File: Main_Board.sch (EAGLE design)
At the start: 52 parts, among them U1 RN4020RN4020, Y1 32KHz, Y2 25MHz

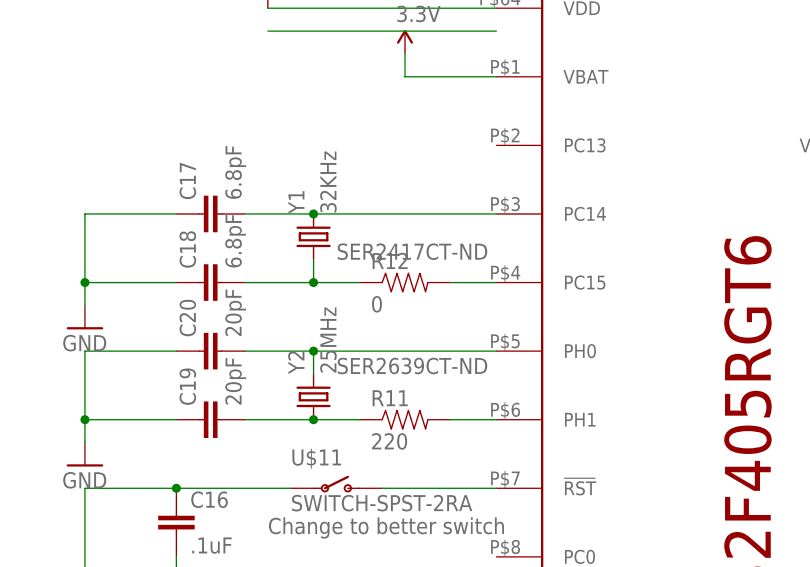
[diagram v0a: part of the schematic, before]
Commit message: added extra oscillator resistor
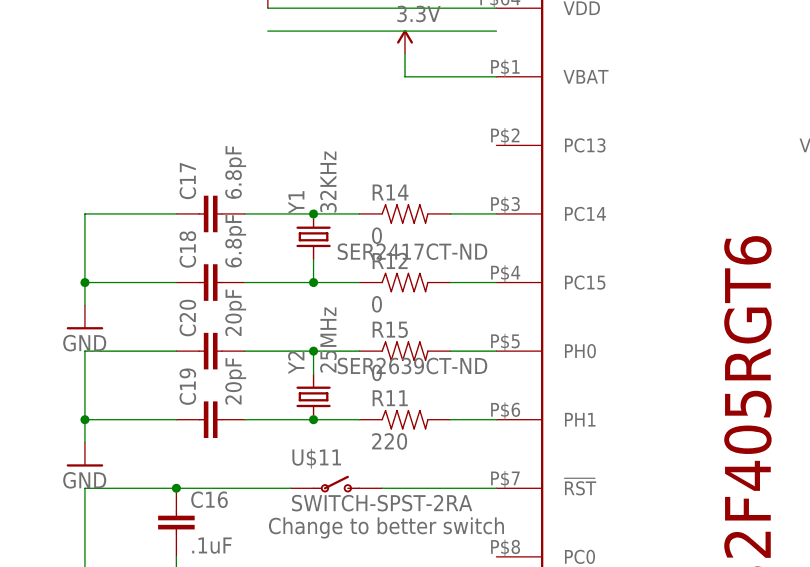
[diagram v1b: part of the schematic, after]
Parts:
- added R14, R15: 0, SparkFun-Passives:RESISTOR0805-RES
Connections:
- new net N$29: R14.2, U$5.PC14
- new net N$30: R15.2, U$5.PH0
- net N$12: now also R14.1; no longer U$5.PC14
- net N$20: now also R15.1; no longer U$5.PH0
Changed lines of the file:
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@@
 <part name="SUPPLY19" library="SparkFun-Aesthetics" deviceset="3.3V" device=""/>
 <part name="GND36" library="SparkFun-Aesthetics" deviceset="GND" device=""/>
+<part name="R14" library="SparkFun-Passives" deviceset="RESISTOR" device="0805-RES" value="0"/>
+<part name="R15" library="SparkFun-Passives" deviceset="RESISTOR" device="0805-RES" value="0"/>
 </parts>
 <sheets>
@@
 <instance part="SUPPLY19" gate="G$1" x="304.8" y="187.96"/>
 <instance part="GND36" gate="1" x="304.8" y="172.72"/>
+<instance part="R14" gate="G$1" x="325.12" y="127"/>
+<instance part="R15" gate="G$1" x="325.12" y="111.76"/>
 </instances>
 <busses>
@@
 <segment>
 <pinref part="Y1" gate="G$1" pin="2"/>
-<pinref part="U$5" gate="G$1" pin="PC14"/>
-<wire x1="314.96" y1="127" x2="335.28" y2="127" width="0.1524" layer="91"/>
 <pinref part="C17" gate="G$1" pin="2"/>
 <wire x1="307.34" y1="127" x2="314.96" y2="127" width="0.1524" layer="91"/>
+<pinref part="R14" gate="G$1" pin="1"/>
+<wire x1="314.96" y1="127" x2="320.04" y2="127" width="0.1524" layer="91"/>
 <junction x="314.96" y="127"/>
 </segment>
@@
 <segment>
 <pinref part="C20" gate="G$1" pin="2"/>
-<pinref part="U$5" gate="G$1" pin="PH0"/>
 <wire x1="307.34" y1="111.76" x2="314.96" y2="111.76" width="0.1524" layer="91"/>
 <pinref part="Y2" gate="G$1" pin="2"/>
-<wire x1="314.96" y1="111.76" x2="335.28" y2="111.76" width="0.1524" layer="91"/>
 <wire x1="314.96" y1="109.22" x2="314.96" y2="111.76" width="0.1524" layer="91"/>
+<pinref part="R15" gate="G$1" pin="1"/>
+<wire x1="320.04" y1="111.76" x2="314.96" y2="111.76" width="0.1524" layer="91"/>
 <junction x="314.96" y="111.76"/>
 </segment>
@@
 </segment>
 </net>
+<net name="N$29" class="0">
+<segment>
+<pinref part="R14" gate="G$1" pin="2"/>
+<pinref part="U$5" gate="G$1" pin="PC14"/>
+<wire x1="330.2" y1="127" x2="335.28" y2="127" width="0.1524" layer="91"/>
+</segment>
+</net>
+<net name="N$30" class="0">
+<segment>
+<pinref part="U$5" gate="G$1" pin="PH0"/>
+<pinref part="R15" gate="G$1" pin="2"/>
+<wire x1="335.28" y1="111.76" x2="330.2" y2="111.76" width="0.1524" layer="91"/>
+</segment>
+</net>

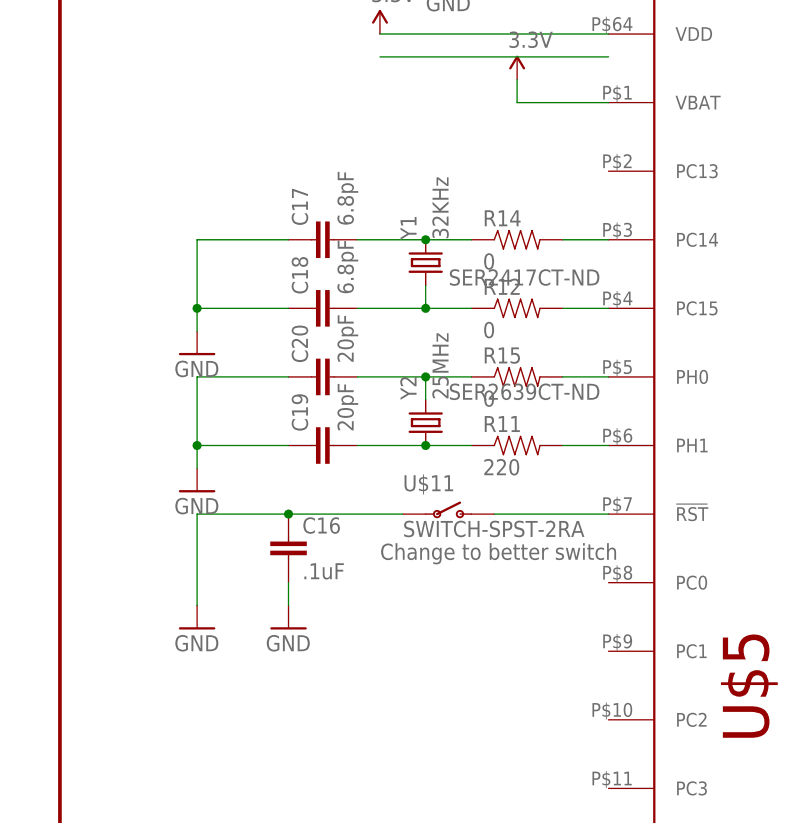
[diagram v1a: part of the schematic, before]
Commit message: updated crystals
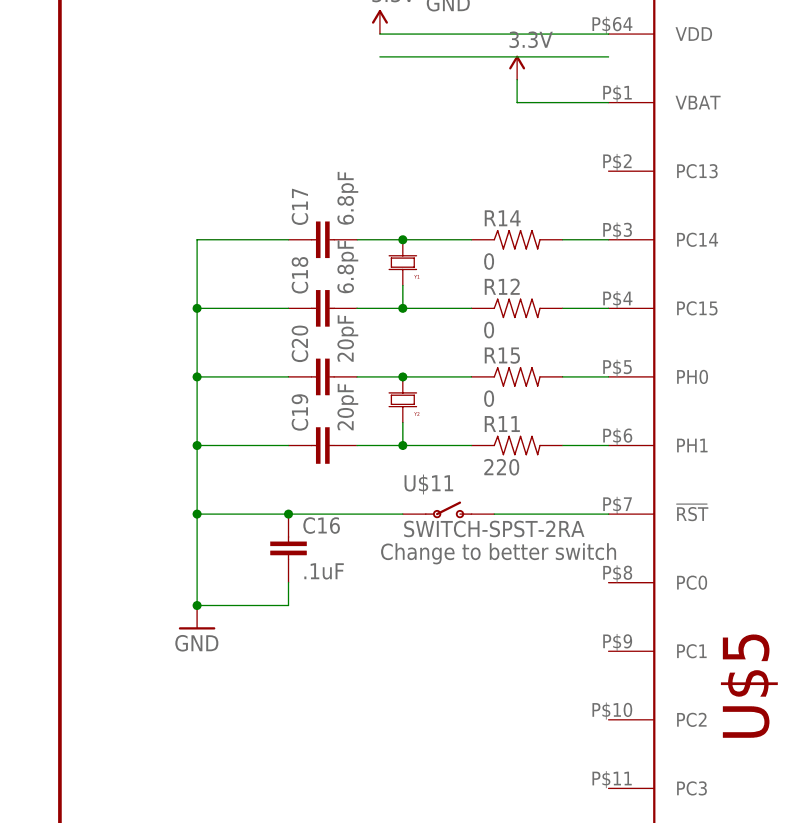
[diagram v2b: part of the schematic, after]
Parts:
- Y1: value 32KHz -> MC-30632.768K-E3; device SparkFun-FreqCtrl:CRYSTALCRYSTAL-SMD-5X3-12MHZ -> BB8:MC-30632.768K-E3
- Y2: value 25MHz -> MA-5066-25.0000M-C0; device SparkFun-FreqCtrl:CRYSTALCRYSTAL-SMD-5X3-12MHZ -> BB8:MA-5066-25.0000M-C0
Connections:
- net N$12: now also Y1.P$1; no longer Y1.2
- net N$17: now also Y2.P$2; no longer Y2.1
- net N$18: now also Y1.P$2; no longer Y1.1
- net N$20: now also Y2.P$1; no longer Y2.2
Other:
- note removed: "SER2417CT-ND"
- note removed: "SER2639CT-ND"
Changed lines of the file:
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@@
 <part name="U$11" library="SparkFun-Electromechanical" deviceset="SWITCH-SPST-2" device="RA"/>
 <part name="C16" library="SparkFun-Passives" deviceset="CAP" device="0805" value=".1uF"/>
-<part name="GND32" library="SparkFun-Aesthetics" deviceset="GND" device=""/>
 <part name="GND33" library="SparkFun-Aesthetics" deviceset="GND" device=""/>
-<part name="Y1" library="SparkFun-FreqCtrl" deviceset="CRYSTAL" device="CRYSTAL-SMD-5X3-12MHZ" value="32KHz"/>
 <part name="C17" library="SparkFun-Passives" deviceset="CAP" device="0805" value="6.8pF"/>
 <part name="C18" library="SparkFun-Passives" deviceset="CAP" device="0805" value="6.8pF"/>
-<part name="GND34" library="SparkFun-Aesthetics" deviceset="GND" device=""/>
-<part name="Y2" library="SparkFun-FreqCtrl" deviceset="CRYSTAL" device="CRYSTAL-SMD-5X3-12MHZ" value="25MHz"/>
 <part name="C19" library="SparkFun-Passives" deviceset="CAP" device="0805" value="20pF"/>
 <part name="C20" library="SparkFun-Passives" deviceset="CAP" device="0805" value="20pF"/>
-<part name="GND35" library="SparkFun-Aesthetics" deviceset="GND" device=""/>
 <part name="R11" library="SparkFun-Passives" deviceset="RESISTOR" device="0805-RES" value="220"/>
 <part name="R12" library="SparkFun-Passives" deviceset="RESISTOR" device="0805-RES" value="0"/>
@@
 <part name="R14" library="SparkFun-Passives" deviceset="RESISTOR" device="0805-RES" value="0"/>
 <part name="R15" library="SparkFun-Passives" deviceset="RESISTOR" device="0805-RES" value="0"/>
+<part name="Y1" library="BB8" deviceset="MC-30632.768K-E3" device=""/>
+<part name="Y2" library="BB8" deviceset="MA-5066-25.0000M-C0" device=""/>
 </parts>
 <sheets>
@@
 MC2_INH_3.3</text>
 <text x="309.88" y="91.44" size="1.778" layer="95">Change to better switch</text>
-<text x="317.5" y="121.92" size="1.778" layer="95">SER2417CT-ND</text>
-<text x="317.5" y="109.22" size="1.778" layer="95">SER2639CT-ND</text>
 </plain>
 <instances>
@@
 <instance part="U$11" gate="G$1" x="317.5" y="96.52"/>
 <instance part="C16" gate="G$1" x="299.72" y="91.44"/>
-<instance part="GND32" gate="1" x="299.72" y="83.82"/>
 <instance part="GND33" gate="1" x="289.56" y="83.82"/>
-<instance part="Y1" gate="G$1" x="314.96" y="124.46" rot="R90"/>
 <instance part="C17" gate="G$1" x="304.8" y="127" rot="R90"/>
 <instance part="C18" gate="G$1" x="304.8" y="119.38" rot="R90"/>
-<instance part="GND34" gate="1" x="289.56" y="114.3"/>
-<instance part="Y2" gate="G$1" x="314.96" y="106.68" rot="R90"/>
 <instance part="C19" gate="G$1" x="304.8" y="104.14" rot="R90"/>
 <instance part="C20" gate="G$1" x="304.8" y="111.76" rot="R90"/>
-<instance part="GND35" gate="1" x="289.56" y="99.06"/>
 <instance part="R11" gate="G$1" x="325.12" y="104.14"/>
 <instance part="R12" gate="G$1" x="325.12" y="119.38"/>
@@
 <instance part="R14" gate="G$1" x="325.12" y="127"/>
 <instance part="R15" gate="G$1" x="325.12" y="111.76"/>
+<instance part="Y1" gate="G$1" x="312.42" y="127"/>
+<instance part="Y2" gate="G$1" x="312.42" y="111.76"/>
 </instances>
 <busses>
@@
 </segment>
 <segment>
-<pinref part="C16" gate="G$1" pin="2"/>
-<pinref part="GND32" gate="1" pin="GND"/>
-<wire x1="299.72" y1="86.36" x2="299.72" y2="88.9" width="0.1524" layer="91"/>
-</segment>
-<segment>
 <pinref part="GND33" gate="1" pin="GND"/>
 <wire x1="289.56" y1="86.36" x2="289.56" y2="96.52" width="0.1524" layer="91"/>
@@
 <wire x1="289.56" y1="96.52" x2="299.72" y2="96.52" width="0.1524" layer="91"/>
 <junction x="299.72" y="96.52"/>
-</segment>
-<segment>
 <pinref part="C17" gate="G$1" pin="1"/>
-<pinref part="GND34" gate="1" pin="GND"/>
 <wire x1="299.72" y1="127" x2="289.56" y2="127" width="0.1524" layer="91"/>
 <wire x1="289.56" y1="127" x2="289.56" y2="119.38" width="0.1524" layer="91"/>
 <pinref part="C18" gate="G$1" pin="1"/>
-<wire x1="289.56" y1="119.38" x2="289.56" y2="116.84" width="0.1524" layer="91"/>
 <wire x1="299.72" y1="119.38" x2="289.56" y2="119.38" width="0.1524" layer="91"/>
 <junction x="289.56" y="119.38"/>
-</segment>
-<segment>
 <pinref part="C20" gate="G$1" pin="1"/>
-<pinref part="GND35" gate="1" pin="GND"/>
 <wire x1="299.72" y1="111.76" x2="289.56" y2="111.76" width="0.1524" layer="91"/>
 <wire x1="289.56" y1="111.76" x2="289.56" y2="104.14" width="0.1524" layer="91"/>
 <pinref part="C19" gate="G$1" pin="1"/>
-<wire x1="289.56" y1="104.14" x2="289.56" y2="101.6" width="0.1524" layer="91"/>
 <wire x1="299.72" y1="104.14" x2="289.56" y2="104.14" width="0.1524" layer="91"/>
 <junction x="289.56" y="104.14"/>
+<wire x1="289.56" y1="119.38" x2="289.56" y2="111.76" width="0.1524" layer="91"/>
+<junction x="289.56" y="111.76"/>
+<wire x1="289.56" y1="104.14" x2="289.56" y2="96.52" width="0.1524" layer="91"/>
+<junction x="289.56" y="96.52"/>
+<pinref part="C16" gate="G$1" pin="2"/>
+<wire x1="299.72" y1="86.36" x2="299.72" y2="88.9" width="0.1524" layer="91"/>
+<wire x1="299.72" y1="86.36" x2="289.56" y2="86.36" width="0.1524" layer="91"/>
+<junction x="289.56" y="86.36"/>
 </segment>
 <segment>
@@
 </segment>
 </net>
-<net name="N$12" class="0">
-<segment>
-<pinref part="Y1" gate="G$1" pin="2"/>
-<pinref part="C17" gate="G$1" pin="2"/>
-<wire x1="307.34" y1="127" x2="314.96" y2="127" width="0.1524" layer="91"/>
-<pinref part="R14" gate="G$1" pin="1"/>
-<wire x1="314.96" y1="127" x2="320.04" y2="127" width="0.1524" layer="91"/>
-<junction x="314.96" y="127"/>
-</segment>
-</net>
-<net name="N$18" class="0">
-<segment>
-<pinref part="Y1" gate="G$1" pin="1"/>
-<wire x1="314.96" y1="119.38" x2="314.96" y2="121.92" width="0.1524" layer="91"/>
-<pinref part="C18" gate="G$1" pin="2"/>
-<wire x1="307.34" y1="119.38" x2="314.96" y2="119.38" width="0.1524" layer="91"/>
-<pinref part="R12" gate="G$1" pin="1"/>
-<wire x1="320.04" y1="119.38" x2="314.96" y2="119.38" width="0.1524" layer="91"/>
-<junction x="314.96" y="119.38"/>
-</segment>
-</net>
 <net name="N$17" class="0">
 <segment>
 <pinref part="C19" gate="G$1" pin="2"/>
-<pinref part="Y2" gate="G$1" pin="1"/>
-<wire x1="307.34" y1="104.14" x2="314.96" y2="104.14" width="0.1524" layer="91"/>
+<wire x1="307.34" y1="104.14" x2="312.42" y2="104.14" width="0.1524" layer="91"/>
 <pinref part="R11" gate="G$1" pin="1"/>
-<wire x1="314.96" y1="104.14" x2="320.04" y2="104.14" width="0.1524" layer="91"/>
-<junction x="314.96" y="104.14"/>
+<pinref part="Y2" gate="G$1" pin="P$2"/>
+<wire x1="312.42" y1="104.14" x2="320.04" y2="104.14" width="0.1524" layer="91"/>
+<wire x1="312.42" y1="106.68" x2="312.42" y2="104.14" width="0.1524" layer="91"/>
+<junction x="312.42" y="104.14"/>
 </segment>
 </net>
@@
 <segment>
 <pinref part="C20" gate="G$1" pin="2"/>
-<wire x1="307.34" y1="111.76" x2="314.96" y2="111.76" width="0.1524" layer="91"/>
-<pinref part="Y2" gate="G$1" pin="2"/>
-<wire x1="314.96" y1="109.22" x2="314.96" y2="111.76" width="0.1524" layer="91"/>
+<wire x1="307.34" y1="111.76" x2="312.42" y2="111.76" width="0.1524" layer="91"/>
 <pinref part="R15" gate="G$1" pin="1"/>
-<wire x1="320.04" y1="111.76" x2="314.96" y2="111.76" width="0.1524" layer="91"/>
-<junction x="314.96" y="111.76"/>
+<pinref part="Y2" gate="G$1" pin="P$1"/>
+<wire x1="312.42" y1="111.76" x2="320.04" y2="111.76" width="0.1524" layer="91"/>
+<junction x="312.42" y="111.76"/>
 </segment>
 </net>
@@
 </segment>
 </net>
+<net name="N$18" class="0">
+<segment>
+<pinref part="C18" gate="G$1" pin="2"/>
+<pinref part="R12" gate="G$1" pin="1"/>
+<wire x1="307.34" y1="119.38" x2="312.42" y2="119.38" width="0.1524" layer="91"/>
+<pinref part="Y1" gate="G$1" pin="P$2"/>
+<wire x1="312.42" y1="119.38" x2="320.04" y2="119.38" width="0.1524" layer="91"/>
+<wire x1="312.42" y1="121.92" x2="312.42" y2="119.38" width="0.1524" layer="91"/>
+<junction x="312.42" y="119.38"/>
+</segment>
+</net>
+<net name="N$12" class="0">
+<segment>
+<pinref part="C17" gate="G$1" pin="2"/>
+<pinref part="Y1" gate="G$1" pin="P$1"/>
+<wire x1="307.34" y1="127" x2="312.42" y2="127" width="0.1524" layer="91"/>
+<pinref part="R14" gate="G$1" pin="1"/>
+<wire x1="320.04" y1="127" x2="312.42" y2="127" width="0.1524" layer="91"/>
+<junction x="312.42" y="127"/>
+</segment>
+</net>

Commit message: added buck regulator
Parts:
- removed S1: (no value), SparkFun-Electromechanical:SWITCH-SPDTPTH_LOCK
- removed U$11: SWITCH-SPST-2RA, SparkFun-Electromechanical:SWITCH-SPST-2RA
- added JP1: SPDT_JUMPER, BB8:SPDT_JUMPER
- added S2: RESET_BUTTON, BB8:RESET_BUTTON
- renumbered U$8 to U2
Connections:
- net 3.3V: now also JP1.S; no longer S1.S
- net GND: now also JP1.O, S2.P; no longer S1.O, U$11.P
- net N$23: now also JP1.P; no longer S1.P
- net N$7: now also S2.O; no longer U$11.O
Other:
- note removed: "Change to better switch"
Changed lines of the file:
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@@
 <part name="GND16" library="SparkFun-Aesthetics" deviceset="GND" device=""/>
 <part name="FRAME2" library="SparkFun-Aesthetics" deviceset="FRAME-LEDGER" device=""/>
-<part name="FRAME4" library="SparkFun-Aesthetics" deviceset="FRAME-LEDGER" device=""/>
 <part name="FRAME1" library="SparkFun-Aesthetics" deviceset="FRAME-LEDGER" device=""/>
 <part name="FRAME3" library="SparkFun-Aesthetics" deviceset="FRAME-LEDGER" device=""/>
-<part name="U$8" library="BB8" deviceset="LMS8117" device=""/>
 <part name="SUPPLY12" library="SparkFun-Aesthetics" deviceset="5V" device=""/>
 <part name="GND17" library="SparkFun-Aesthetics" deviceset="GND" device=""/>
@@
 <part name="GND30" library="SparkFun-Aesthetics" deviceset="GND" device=""/>
 <part name="GND31" library="SparkFun-Aesthetics" deviceset="GND" device=""/>
-<part name="U$11" library="SparkFun-Electromechanical" deviceset="SWITCH-SPST-2" device="RA"/>
 <part name="C16" library="SparkFun-Passives" deviceset="CAP" device="0805" value=".1uF"/>
 <part name="GND33" library="SparkFun-Aesthetics" deviceset="GND" device=""/>
@@
 <part name="R11" library="SparkFun-Passives" deviceset="RESISTOR" device="0805-RES" value="220"/>
 <part name="R12" library="SparkFun-Passives" deviceset="RESISTOR" device="0805-RES" value="0"/>
-<part name="S1" library="SparkFun-Electromechanical" deviceset="SWITCH-SPDT" device="PTH_LOCK"/>
 <part name="R13" library="SparkFun-Passives" deviceset="RESISTOR" device="0805-RES" value="10K"/>
 <part name="SUPPLY19" library="SparkFun-Aesthetics" deviceset="3.3V" device=""/>
@@
 <part name="Y1" library="BB8" deviceset="MC-30632.768K-E3" device=""/>
 <part name="Y2" library="BB8" deviceset="MA-5066-25.0000M-C0" device=""/>
+<part name="S2" library="BB8" deviceset="RESET_BUTTON" device=""/>
+<part name="JP1" library="BB8" deviceset="SPDT_JUMPER" device=""/>
+<part name="FRAME4" library="SparkFun-Aesthetics" deviceset="FRAME-LEDGER" device=""/>
+<part name="U2" library="BB8" deviceset="LMS8117" device=""/>
 </parts>
 <sheets>
@@
 MC1_INH_3.3
 MC2_INH_3.3</text>
-<text x="309.88" y="91.44" size="1.778" layer="95">Change to better switch</text>
 </plain>
 <instances>
@@
 <instance part="FRAME2" gate="G$1" x="274.32" y="-45.72"/>
 <instance part="FRAME2" gate="G$2" x="604.52" y="-45.72"/>
-<instance part="FRAME4" gate="G$1" x="-172.72" y="-43.18"/>
-<instance part="FRAME4" gate="G$2" x="157.48" y="-43.18"/>
 <instance part="FRAME1" gate="G$1" x="-170.18" y="-335.28"/>
 <instance part="FRAME1" gate="G$2" x="157.48" y="-332.74"/>
 <instance part="FRAME3" gate="G$1" x="274.32" y="-335.28"/>
 <instance part="FRAME3" gate="G$2" x="601.98" y="-335.28"/>
-<instance part="U$8" gate="G$1" x="-104.14" y="-93.98"/>
 <instance part="SUPPLY12" gate="G$1" x="-129.54" y="-88.9"/>
 <instance part="GND17" gate="1" x="-129.54" y="-106.68"/>
@@
 <instance part="GND30" gate="1" x="538.48" y="-157.48"/>
 <instance part="GND31" gate="1" x="566.42" y="-165.1"/>
-<instance part="U$11" gate="G$1" x="317.5" y="96.52"/>
 <instance part="C16" gate="G$1" x="299.72" y="91.44"/>
 <instance part="GND33" gate="1" x="289.56" y="83.82"/>
@@
 <instance part="R11" gate="G$1" x="325.12" y="104.14"/>
 <instance part="R12" gate="G$1" x="325.12" y="119.38"/>
-<instance part="S1" gate="1" x="312.42" y="180.34" rot="R180"/>
 <instance part="R13" gate="G$1" x="325.12" y="180.34"/>
 <instance part="SUPPLY19" gate="G$1" x="304.8" y="187.96"/>
@@
 <instance part="Y1" gate="G$1" x="312.42" y="127"/>
 <instance part="Y2" gate="G$1" x="312.42" y="111.76"/>
+<instance part="S2" gate="G$1" x="317.5" y="96.52"/>
+<instance part="JP1" gate="G$1" x="312.42" y="180.34" rot="R180"/>
+<instance part="FRAME4" gate="G$1" x="-175.26" y="-43.18"/>
+<instance part="FRAME4" gate="G$2" x="154.94" y="-43.18"/>
+<instance part="U2" gate="G$1" x="-104.14" y="-93.98"/>
 </instances>
 <busses>
@@
 <segment>
 <pinref part="C13" gate="G$1" pin="2"/>
-<pinref part="U$8" gate="G$1" pin="ADJ/GND"/>
 <wire x1="-124.46" y1="-101.6" x2="-109.22" y2="-101.6" width="0.1524" layer="91"/>
 <pinref part="GND17" gate="1" pin="GND"/>
@@
 <wire x1="-129.54" y1="-101.6" x2="-124.46" y2="-101.6" width="0.1524" layer="91"/>
 <junction x="-124.46" y="-101.6"/>
+<pinref part="U2" gate="G$1" pin="ADJ/GND"/>
 </segment>
 <segment>
@@
 <pinref part="GND33" gate="1" pin="GND"/>
 <wire x1="289.56" y1="86.36" x2="289.56" y2="96.52" width="0.1524" layer="91"/>
-<pinref part="U$11" gate="G$1" pin="P"/>
 <pinref part="C16" gate="G$1" pin="1"/>
 <wire x1="312.42" y1="96.52" x2="299.72" y2="96.52" width="0.1524" layer="91"/>
@@
 <wire x1="299.72" y1="86.36" x2="289.56" y2="86.36" width="0.1524" layer="91"/>
 <junction x="289.56" y="86.36"/>
-</segment>
-<segment>
-<pinref part="S1" gate="1" pin="O"/>
+<pinref part="S2" gate="G$1" pin="P"/>
+</segment>
+<segment>
 <pinref part="GND36" gate="1" pin="GND"/>
 <wire x1="307.34" y1="177.8" x2="304.8" y2="177.8" width="0.1524" layer="91"/>
 <wire x1="304.8" y1="177.8" x2="304.8" y2="175.26" width="0.1524" layer="91"/>
+<pinref part="JP1" gate="G$1" pin="O"/>
 </segment>
 </net>
@@
 </segment>
 <segment>
-<pinref part="U$8" gate="G$1" pin="VIN"/>
 <pinref part="C13" gate="G$1" pin="1"/>
 <wire x1="-109.22" y1="-93.98" x2="-124.46" y2="-93.98" width="0.1524" layer="91"/>
@@
 <wire x1="-129.54" y1="-93.98" x2="-129.54" y2="-88.9" width="0.1524" layer="91"/>
 <junction x="-124.46" y="-93.98"/>
+<pinref part="U2" gate="G$1" pin="VIN"/>
 </segment>
 <segment>
@@
 </segment>
 <segment>
-<pinref part="U$8" gate="G$1" pin="VOUT"/>
 <pinref part="C14" gate="G$1" pin="1"/>
 <wire x1="-81.28" y1="-93.98" x2="-71.12" y2="-93.98" width="0.1524" layer="91"/>
@@
 <wire x1="-71.12" y1="-93.98" x2="-71.12" y2="-91.44" width="0.1524" layer="91"/>
 <junction x="-71.12" y="-93.98"/>
+<pinref part="U2" gate="G$1" pin="VOUT"/>
 </segment>
 <segment>
@@
 </segment>
 <segment>
-<pinref part="S1" gate="1" pin="S"/>
 <pinref part="SUPPLY19" gate="G$1" pin="3.3V"/>
 <wire x1="307.34" y1="182.88" x2="304.8" y2="182.88" width="0.1524" layer="91"/>
 <wire x1="304.8" y1="182.88" x2="304.8" y2="187.96" width="0.1524" layer="91"/>
+<pinref part="JP1" gate="G$1" pin="S"/>
 </segment>
 </net>
@@
 <segment>
 <pinref part="U$5" gate="G$1" pin="!RST"/>
-<pinref part="U$11" gate="G$1" pin="O"/>
 <wire x1="335.28" y1="96.52" x2="322.58" y2="96.52" width="0.1524" layer="91"/>
+<pinref part="S2" gate="G$1" pin="O"/>
 </segment>
 </net>
@@
 <segment>
 <pinref part="R13" gate="G$1" pin="1"/>
-<pinref part="S1" gate="1" pin="P"/>
 <wire x1="320.04" y1="180.34" x2="314.96" y2="180.34" width="0.1524" layer="91"/>
-</segment>
-</net>
+<pinref part="JP1" gate="G$1" pin="P"/>
+</segment>
+</net>
